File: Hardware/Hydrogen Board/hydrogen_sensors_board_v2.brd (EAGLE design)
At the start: 68.2 x 66 mm, 38 parts, among them U1 ATMEGA328P_TQFP, Y1 16MHz

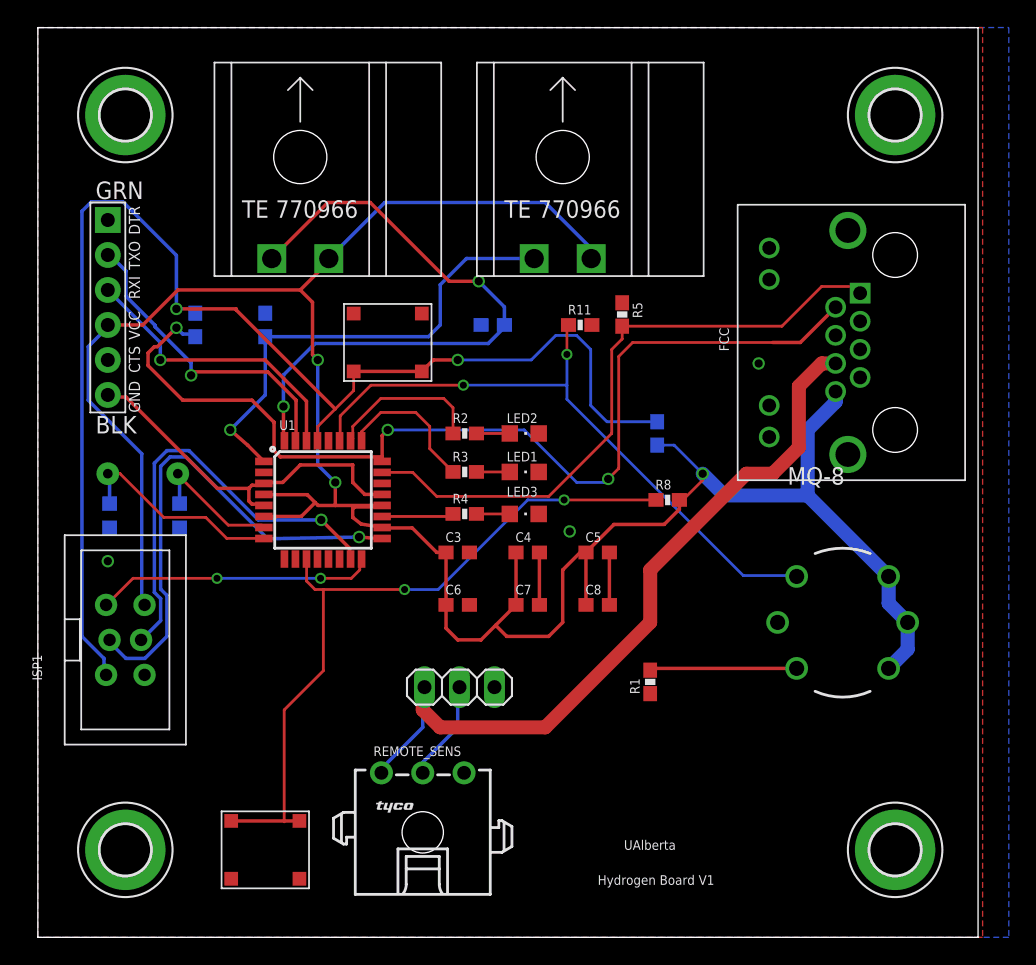
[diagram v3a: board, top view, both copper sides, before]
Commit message: added 3.3V LDO (chip and all digital signals are all 3.3V now). Added appropriate voltage divider for hydrogen sensor output (with optional cap)
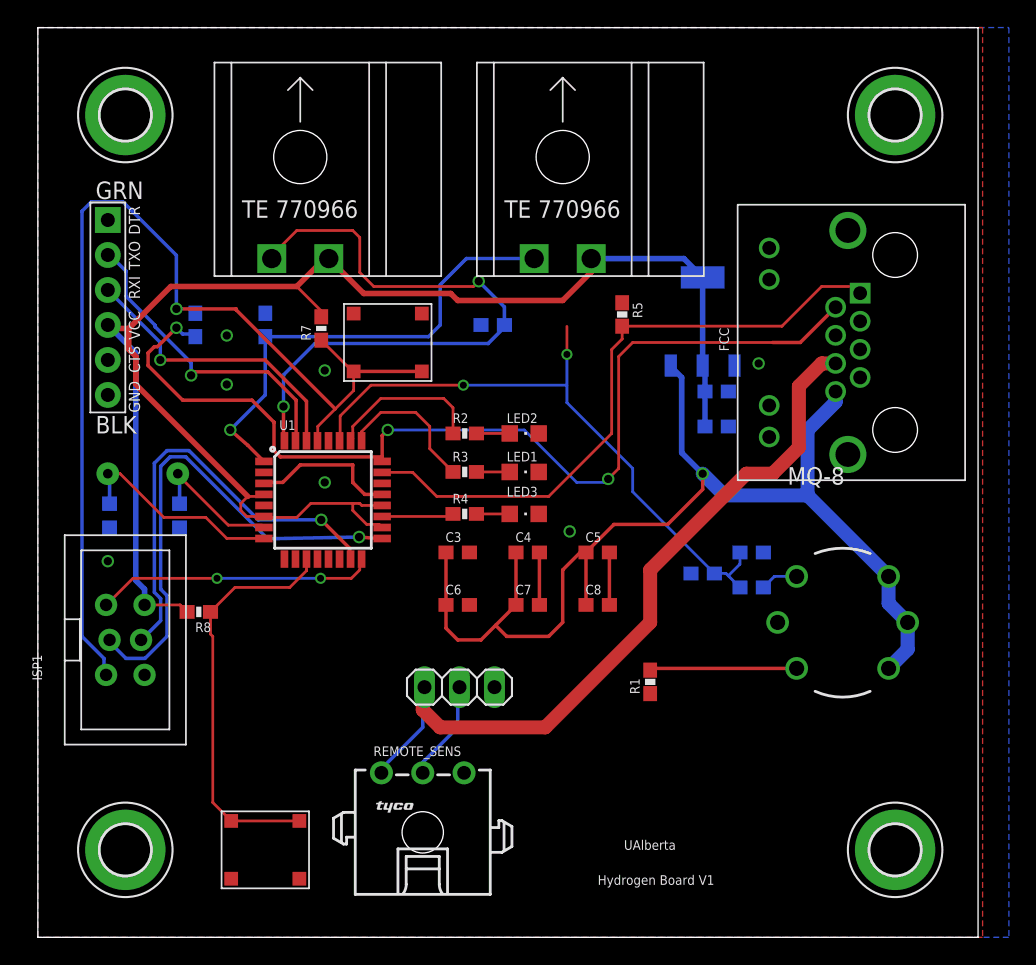
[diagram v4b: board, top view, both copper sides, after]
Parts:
- removed R11: 100k, SparkFun-Resistors:0603-RES
- added C10: 10nF, adafruit:C0603
- added C11, C9: 100nF, adafruit:C0603
- added R12: 20k, SparkFun-Passives:0603-RES
- added R13: 40k, SparkFun-Passives:0603-RES
- added U2: TLV1117-33IDCY, Texas Instruments_By_element14_Batch_1:SOT230P700X180-4N
- moved R8 35.0 mm to (11.7, 23.6), turned to 180 degrees
- moved R7 25.5 mm to (20.6, 44.2), flipped to the top, turned to 90 degrees
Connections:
- new net +3.3V: C10.1, C9.1, ISP1.2, JP6.P$4, R7.2, R8.2, U$3.CIRCUIT1, U$9.CIRCUIT1, U1.18, U1.20, U1.4, U1.6, U2.2, U2.4
- new net N$10: R12.2, U$1.1
- net +5V: now also U2.3; no longer ISP1.2, JP6.P$4, R7.2, R8.2, U$3.CIRCUIT1, U$9.CIRCUIT1, U1.18, U1.20, U1.4, U1.6
- net GND: now also C10.2, C11.2, C9.2, R13.1, U2.1; no longer R11.2
- net H2OUT: now also C11.1, R12.1, R13.2; no longer R11.1, U$1.1
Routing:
- net +3.3V: track 0.00 -> 119.9 mm
- net +5V: track 183.9 -> 84.4 mm, vias 3 -> 1
- net TARE: track 52.9 -> 29.8 mm, vias 2 -> 0
- net ATM_RESET: track 95.9 -> 76.0 mm, vias 2 -> 1
- net GND: track 34.8 -> 18.4 mm, vias 3 -> 7
- net N$10: track 0.00 -> 2.75 mm
- net H2OUT: track 46.7 -> 45.9 mm
